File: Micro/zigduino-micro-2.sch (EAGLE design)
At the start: 49 parts, among them J2 USB-MINI-B, Q1 AMB8G, Q2 ABS10, Q3 BSS84, U1 ATMEGA1284RFR2, U2 USD-SOCKETNEW, U3 MCP73831, U4 MCP1804-5002I/OT, U5 MCP1804-3302I/OT

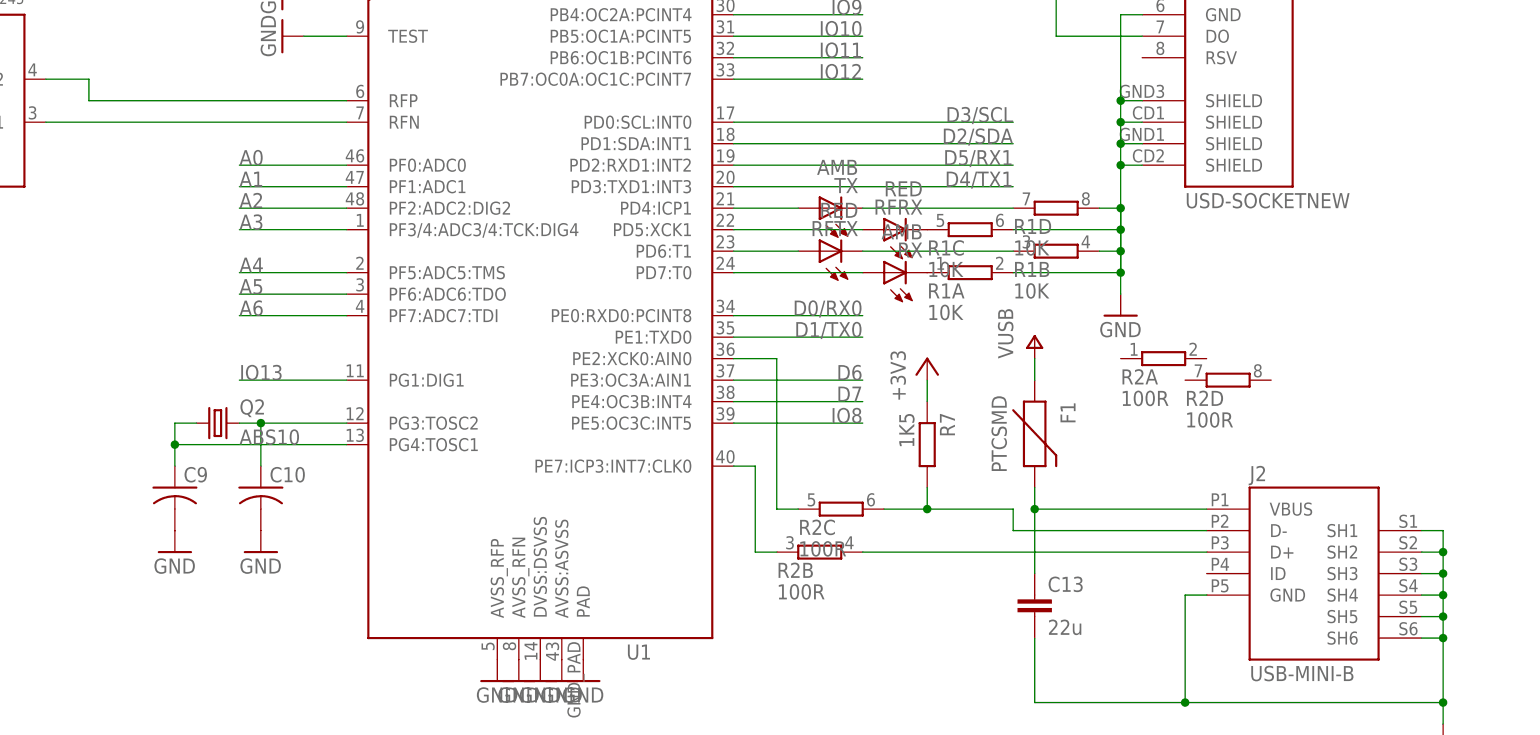
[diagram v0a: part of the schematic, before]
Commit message: added Zigduino Micro files updated burning instructions added Zigduino r3 files
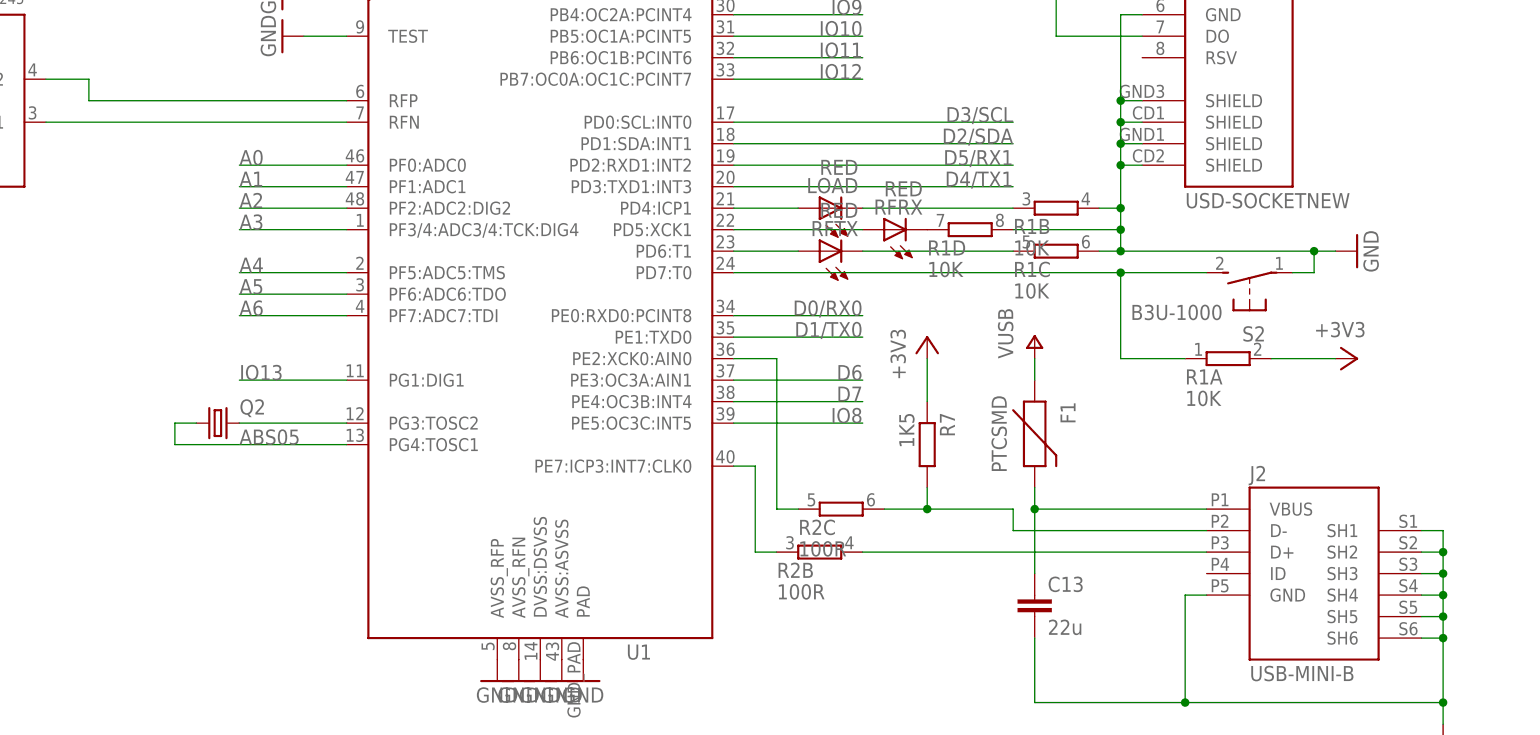
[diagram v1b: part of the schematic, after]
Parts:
- removed C10, C9: (no value), resistor:C-USC0402
- removed RX: AMB, led:LEDCHIPLED_0603
- added S2: B3U-1000, logos-faves:B3U-1000
- C1, C11, C12, C14, C15, C16, C17, C2, C3, C4, C5, C6, C7, C8: device resistor:C-USC0402 -> resistor:C-USC0603
- LOAD: value AMB -> RED
- Q2: value ABS10 -> ABS05; device logos-crystals:ABS10 -> logos-crystals:ABS05
- R3, R4, R5, R6, R7, R8: device resistor:R-EU_R0402 -> resistor:R-EU_R0603
- renumbered TX to LOAD
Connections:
- removed net N$11 (its old number): RX.A, U1.PD7:T0
- removed net N$24: LOAD.C, R1D.1
- new net N$22: R1A.1, S2.2, U1.PD7:T0
- net +3V3: now also R1A.2
- net GND: now also S2.1; no longer C10.2, C9.2, R1A.2
- net N$17: now also R1D.1; no longer R1C.1
- net N$18: now also R1C.1; no longer R1B.1
- net N$21: now also LOAD.C, R1B.1; no longer R1A.1, RX.C
- net N$6: no longer C10.1
- net N$9: no longer C9.1
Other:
- moved on the sheet: R1A, R1B, R1C, R1D
